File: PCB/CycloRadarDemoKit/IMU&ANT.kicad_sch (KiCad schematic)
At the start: 20 parts, among them J101 JTAG, U302 D52MxxM8, U501 MPU-6050, U502 LSM6DSM

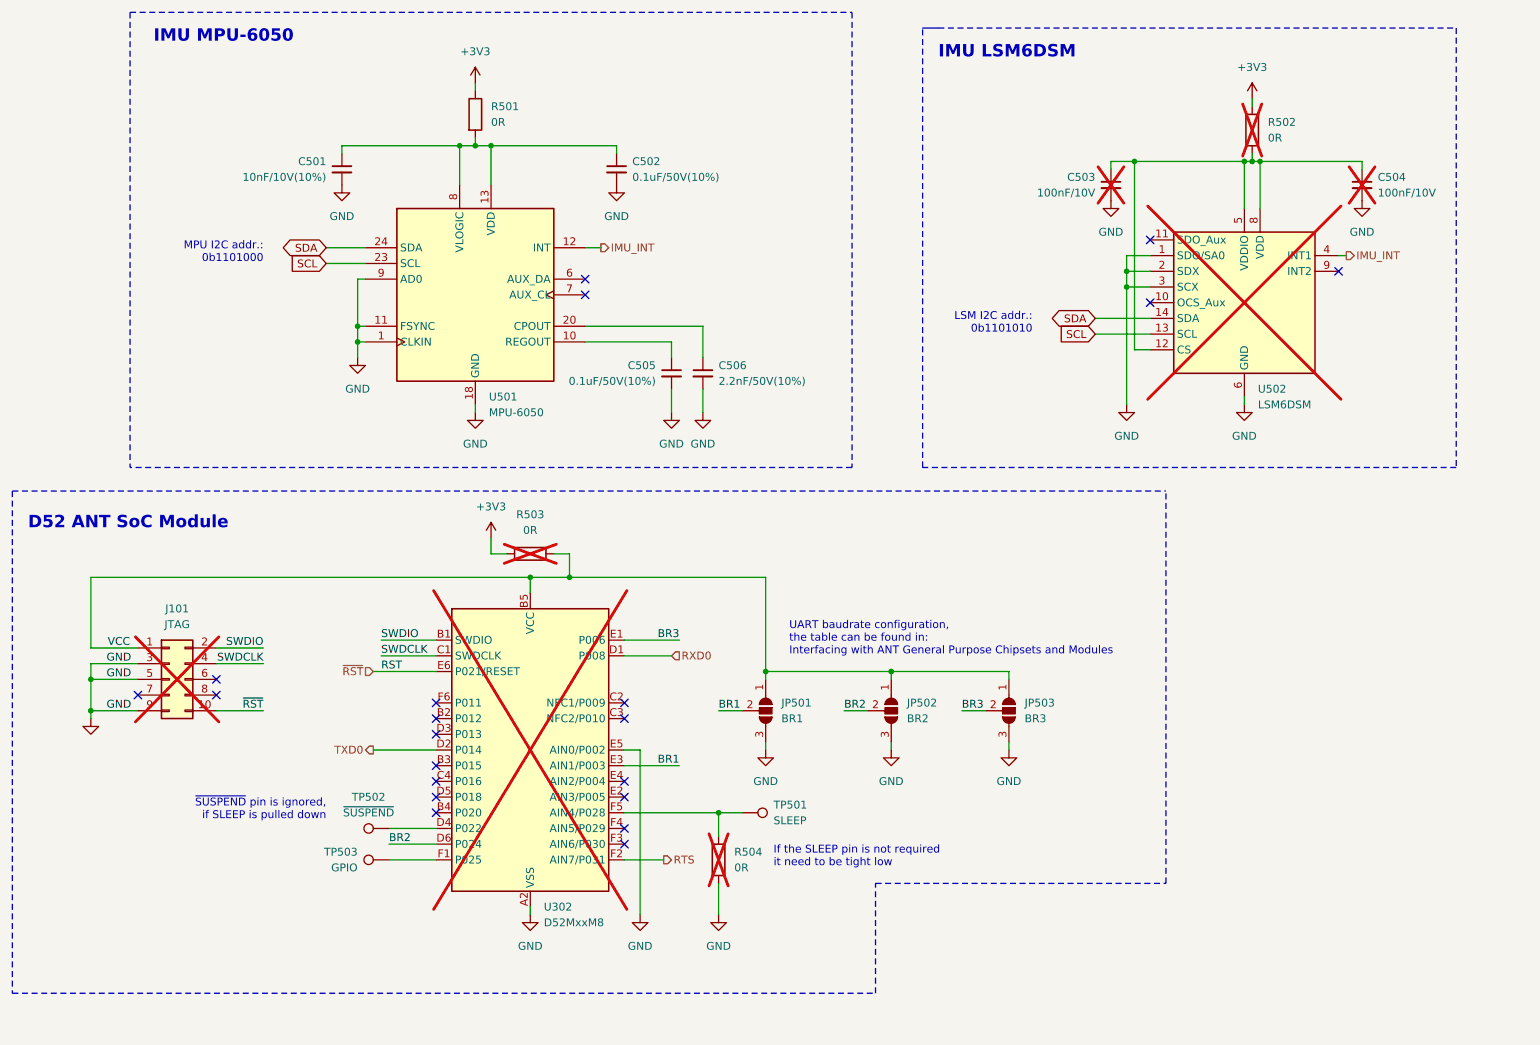
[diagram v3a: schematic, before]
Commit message: added more LCSC parts
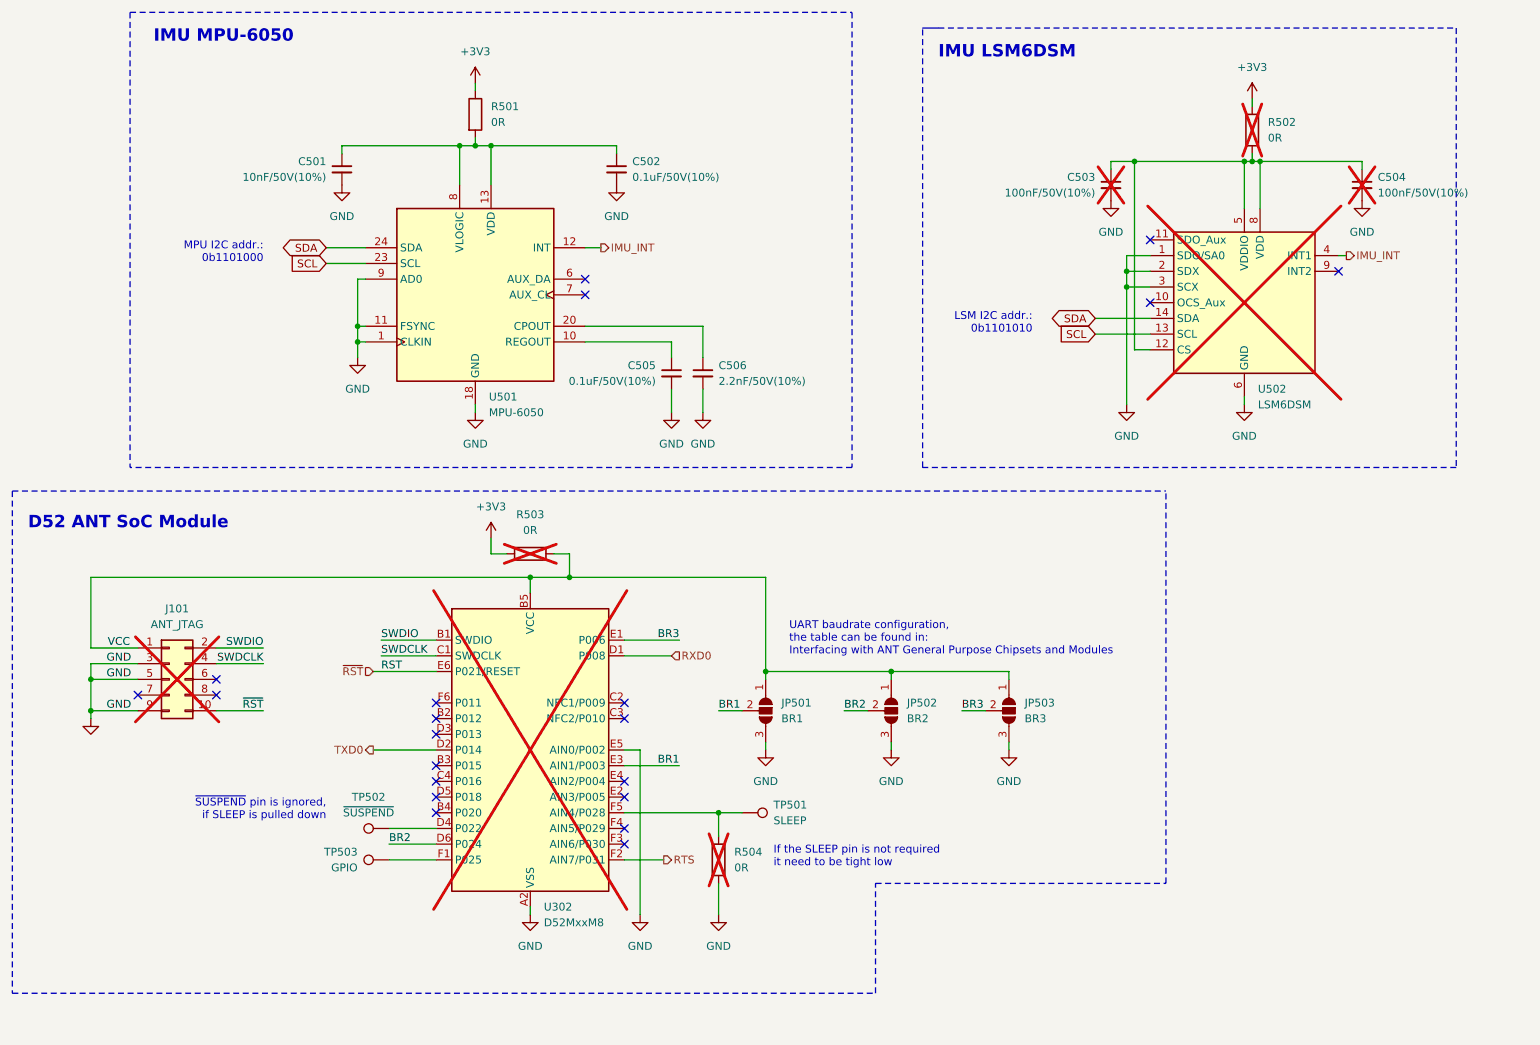
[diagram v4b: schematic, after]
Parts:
- C501: value 10nF/10V(10%) -> 10nF/50V(10%); footprint (none) -> Capacitor_SMD:C_0603_1608Metric; LCSC (none) -> C57112
- C503, C504: value 100nF/10V -> 100nF/50V(10%); footprint (none) -> Capacitor_SMD:C_0805_2012Metric; LCSC (none) -> C2929181
- C506: footprint (none) -> Capacitor_SMD:C_0603_1608Metric; LCSC (none) -> C1604
- J101: value JTAG -> ANT_JTAG
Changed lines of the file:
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@@
       (effects (font (size 1.27 1.27)) (justify left))
     )
-    (property "Value" "100nF/10V" (at 246.38 49.5363 0)
-      (effects (font (size 1.27 1.27)) (justify left))
-    )
-    (property "Footprint" "" (at 243.84 48.26 0)
+    (property "Value" "100nF/50V(10%)" (at 246.38 49.5363 0)
+      (effects (font (size 1.27 1.27)) (justify left))
+    )
+    (property "Footprint" "Capacitor_SMD:C_0805_2012Metric" (at 243.84 48.26 0)
       (effects (font (size 1.27 1.27)) hide)
     )
     (property "Datasheet" "~" (at 243.84 48.26 0)
+      (effects (font (size 1.27 1.27)) hide)
+    )
+    (property "LCSC" "C2929181" (at 243.84 48.26 0)
       (effects (font (size 1.27 1.27)) hide)
     )
@@
       (effects (font (size 1.27 1.27)) (justify left))
     )
-    (property "Value" "100nF/10V" (at 200.66 49.5363 0)
-      (effects (font (size 1.27 1.27)) (justify left))
-    )
-    (property "Footprint" "" (at 203.2 48.26 0)
+    (property "Value" "100nF/50V(10%)" (at 200.66 49.5363 0)
+      (effects (font (size 1.27 1.27)) (justify left))
+    )
+    (property "Footprint" "Capacitor_SMD:C_0805_2012Metric" (at 203.2 48.26 0)
       (effects (font (size 1.27 1.27)) hide)
     )
     (property "Datasheet" "~" (at 203.2 48.26 0)
+      (effects (font (size 1.27 1.27)) hide)
+    )
+    (property "LCSC" "C2929181" (at 203.2 48.26 0)
       (effects (font (size 1.27 1.27)) hide)
     )
@@
       (effects (font (size 1.27 1.27)) (justify left))
     )
-    (property "Value" "10nF/10V(10%)" (at 76.2 46.9963 0)
-      (effects (font (size 1.27 1.27)) (justify left))
-    )
-    (property "Footprint" "" (at 78.74 45.72 0)
+    (property "Value" "10nF/50V(10%)" (at 76.2 46.9963 0)
+      (effects (font (size 1.27 1.27)) (justify left))
+    )
+    (property "Footprint" "Capacitor_SMD:C_0603_1608Metric" (at 78.74 45.72 0)
       (effects (font (size 1.27 1.27)) hide)
     )
@@
       (effects (font (size 1.27 1.27)) hide)
     )
+    (property "LCSC" "C57112" (at 78.74 45.72 0)
+      (effects (font (size 1.27 1.27)) hide)
+    )
     (pin "2")
     (pin "1")
@@
       (effects (font (size 1.27 1.27)) (justify left))
     )
-    (property "Footprint" "" (at 137.16 78.74 0)
+    (property "Footprint" "Capacitor_SMD:C_0603_1608Metric" (at 137.16 78.74 0)
       (effects (font (size 1.27 1.27)) hide)
     )
     (property "Datasheet" "~" (at 137.16 78.74 0)
+      (effects (font (size 1.27 1.27)) hide)
+    )
+    (property "LCSC" "C1604" (at 137.16 78.74 0)
       (effects (font (size 1.27 1.27)) hide)
     )
@@
       (effects (font (size 1.27 1.27)))
     )
-    (property "Value" "JTAG" (at 52.07 119.38 0)
-      (effects (font (size 1.27 1.27)))
-    )
+    (property "Value" "ANT_JTAG" (at 52.07 119.38 0)
+      (effects (font (size 1.27 1.27)))
+    )

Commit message: PCB ready for review
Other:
- note added: "If the SLEEP pin is not required, it need to be tight low"
- note removed: "If the SLEEP pin is not required it need to be tight low"
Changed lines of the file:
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@@
     (effects (font (size 2 2) (thickness 0.4) bold) (justify left bottom))
   )
-  (text "If the SLEEP pin is not required \nit need to be tight low"
+  (text "If the SLEEP pin is not required,\nit need to be tight low"
     (at 148.59 158.75 0)
     (effects (font (size 1.27 1.27)) (justify left bottom))

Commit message: PCB after review
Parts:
- removed C503, C504: 100nF/50V(10%), Capacitor_SMD:C_0805_2012Metric, symbol Device:C_Small
- removed JP502: BR2, Jumper:SolderJumper-3_P1.3mm_Open_RoundedPad1.0x1.5mm_NumberLabels, symbol Jumper:SolderJumper_3_Open
- removed JP503: BR3, Jumper:SolderJumper-3_P1.3mm_Open_RoundedPad1.0x1.5mm_NumberLabels, symbol Jumper:SolderJumper_3_Open
- removed R501, R502: 0R, Resistor_SMD:R_0805_2012Metric, symbol Device:R
- removed U502: LSM6DSM, Package_LGA:LGA-14_3x2.5mm_P0.5mm_LayoutBorder3x4y, symbol Sensor_Motion:LSM6DSM
- added C103: 100nF/50V(10%), Capacitor_SMD:C_0603_1608Metric, symbol Device:C_Small
- added FB301: YI160808Z101-3R0T, Resistor_SMD:R_0603_1608Metric, symbol Device:FerriteBead_Small
- added JP502: BR2, Jumper:SolderJumper-3_P1.3mm_Bridged12_RoundedPad1.0x1.5mm_NumberLabels, symbol Jumper:SolderJumper_3_Bridged12
- added JP503: BR3, Jumper:SolderJumper-3_P1.3mm_Bridged12_RoundedPad1.0x1.5mm_NumberLabels, symbol Jumper:SolderJumper_3_Bridged12
- added R103: 10K(1%), Resistor_SMD:R_0603_1608Metric, symbol Device:R
- C501: footprint Capacitor_SMD:C_0603_1608Metric -> Capacitor_SMD:C_0402_1005Metric; LCSC C57112 -> C15195
- C502, C505: value 0.1uF/50V(10%) -> 100nF/50V(10%)
- JP501: footprint Jumper:SolderJumper-3_P1.3mm_Open_RoundedPad1.0x1.5mm_NumberLabels -> Jumper:SolderJumper-3_P1.3mm_Bridged12_RoundedPad1.0x1.5mm_NumberLabels; symbol Jumper:SolderJumper_3_Open -> Jumper:SolderJumper_3_Bridged12
- TP501, TP502, TP503: footprint (none) -> TestPoint:TestPoint_Pad_D2.0mm
- renumbered R503 to R502, R504 to R503
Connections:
- net +3V3: now also FB301.2
- net BR2: now also JP502.2 (C)
- net BR3: now also JP503.2 (C)
- net GND: now also JP501.1 (A), C103.2, JP502.3 (B), JP503.1 (A); no longer JP501.3 (B)
- net VCC: now also JP501.3 (B), JP502.1 (A), JP503.3 (B), R103.2; no longer JP501.1 (A)
- net ~{RST}: now also C103.1, R103.1
- net at C501.1, C502.1, U501.13 (VDD)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: now also FB301.1
- no-connect marks 21 -> 18
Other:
- note added: "RC = 1ms"
- note added: "Register INT_PIN_CFG bit INT_OPEN must be 1, than pin is open-drain"
- note added: "UART baudrate configuration, default 19200 the table can be found in: Interfacing with ANT General Purpose Chipsets and Modules"
- note removed: "IMU LSM6DSM"
- note removed: "LSM I2C addr.: 0b1101010"
- note removed: "UART baudrate configuration, the table can be found in: Interfacing with ANT General Purpose Chipsets and Modules"
- company: (none) -> ALPS Electric Czech, s.r.o.
- title: (none) -> Safety Ride Radar Sensor
- moved on the sheet: C501, C502, C505, C506, J101, R502, R503, TP501, TP502, TP503, U302, U501

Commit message: Schematic edited, split sheets
improved PM diagram
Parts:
- renumbered C501 to C502, C502 to C503, C505 to C504, C506 to C505, R502 to R501, U501 to U502

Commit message: layout mockup done
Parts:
- C103, R103: now not fitted
- TP501, TP502, TP503: footprint TestPoint:TestPoint_Pad_D2.0mm -> TestPoint:TestPoint_Pad_D1.0mm
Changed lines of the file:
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@@
   )
   (symbol (lib_id "Device:C_Small") (at 121.92 57.15 0) (unit 1)
-    (in_bom yes) (on_board yes) (dnp no) (fields_autoplaced)
+    (in_bom yes) (on_board yes) (dnp yes) (fields_autoplaced)
     (property "Reference" "C103" (at 124.46 55.8863 0)
       (effects (font (size 1.27 1.27)) (justify left))
@@
       (effects (font (size 1.27 1.27)) (justify left))
     )
-    (property "Footprint" "TestPoint:TestPoint_Pad_D2.0mm" (at 135.89 78.74 0)
+    (property "Footprint" "TestPoint:TestPoint_Pad_D1.0mm" (at 135.89 78.74 0)
       (effects (font (size 1.27 1.27)) hide)
     )
@@
       (effects (font (size 1.27 1.27)) (justify left))
     )
-    (property "Footprint" "TestPoint:TestPoint_Pad_D2.0mm" (at 193.04 81.28 0)
+    (property "Footprint" "TestPoint:TestPoint_Pad_D1.0mm" (at 193.04 81.28 0)
       (effects (font (size 1.27 1.27)) hide)
     )
@@
       (effects (font (size 1.27 1.27)))
     )
-    (property "Footprint" "TestPoint:TestPoint_Pad_D2.0mm" (at 135.89 73.66 0)
+    (property "Footprint" "TestPoint:TestPoint_Pad_D1.0mm" (at 135.89 73.66 0)
       (effects (font (size 1.27 1.27)) hide)
     )
@@
   )
   (symbol (lib_id "Device:R") (at 121.92 46.99 0) (mirror x) (unit 1)
-    (in_bom yes) (on_board yes) (dnp no) (fields_autoplaced)
+    (in_bom yes) (on_board yes) (dnp yes) (fields_autoplaced)
     (property "Reference" "R103" (at 124.46 45.72 0)
       (effects (font (size 1.27 1.27)) (justify left))
